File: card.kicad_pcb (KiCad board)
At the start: 2 copper layers, 38.6 x 52.3 mm, 91 parts, among them J1 Conn_01x20_Male, J2 HDMI_A, J3 Conn_01x20_Male, J4 USB_B_Micro, Q1 MMBT3906, Q3 MMBT3906, Q4 MMBT3904, SW1 SW_DPST_x2, U1 SPX3819-1.8, U2 IMP811REUS-T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

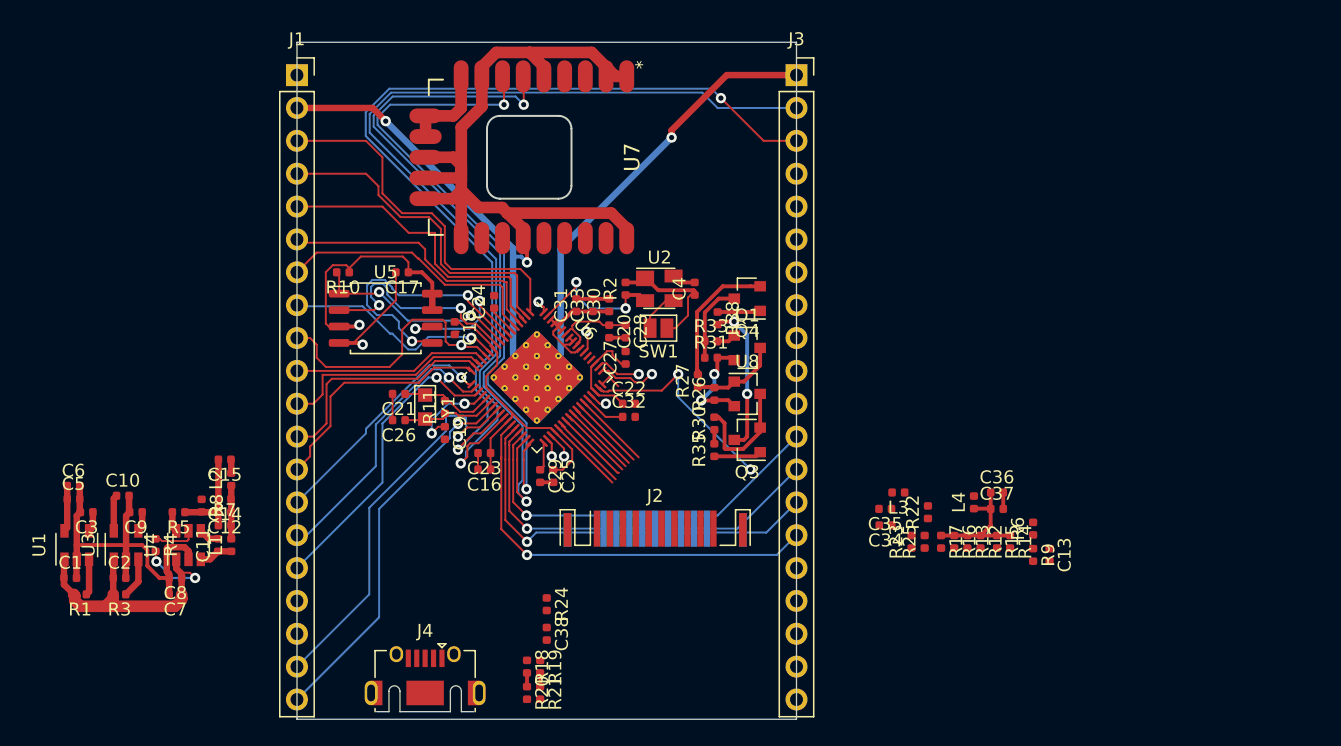
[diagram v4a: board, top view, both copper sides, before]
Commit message: removed USB power protection. did more routing
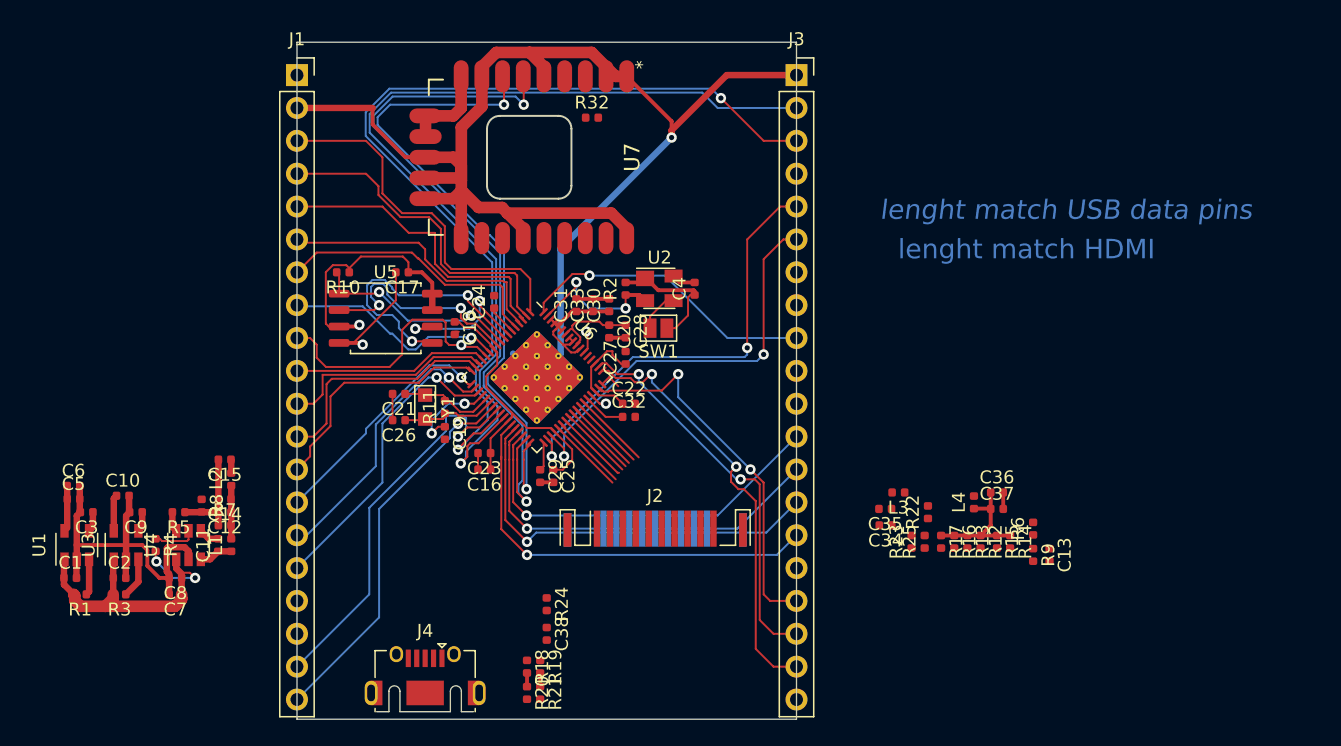
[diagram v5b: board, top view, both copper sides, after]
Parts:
- removed Q1, Q3: MMBT3906, Package_TO_SOT_SMD:SOT-23
- removed Q4: MMBT3904, Package_TO_SOT_SMD:SOT-23
- removed R26: 100k, Resistor_SMD:R_0402_1005Metric
- removed R27, R31: 10k, Resistor_SMD:R_0402_1005Metric
- removed R30: 0.5R, Resistor_SMD:R_0402_1005Metric
- removed R33, R35, R38: 510R, Resistor_SMD:R_0402_1005Metric
- removed U8: SLS2301, Package_TO_SOT_SMD:SOT-23
- added R32: 510R, Resistor_SMD:R_0402_1005Metric, F.Cu at (256.7, 62.5)
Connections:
- J3 pad 16: IR -> (no net)
- J3 pad 17: GND -> VOUT1
- J3 pad 18: VOUT1 -> AOR
- J3 pad 19: AOR -> AOL
- J3 pad 20: AOL -> GND
- J3 pad 4: USB2-VCC -> +5V
- J3 pad 8: (no net) -> GND
- J3 pad 9: (no net) -> IR
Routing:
- net HOST1_DP: track 1.48 -> 34.2 mm, vias 1 -> 2
- net HOST1_DM: track 2.04 -> 32.0 mm, vias 1 -> 2
- net AOL: track 4.47 -> 33.1 mm, vias 1 -> 2
- net AOR: track 3.58 -> 30.3 mm, vias 1 -> 2
- net GND: track 194.2 -> 169.5 mm, vias 4 -> 2
- net IR: track 0.96 -> 23.0 mm
- net VOUT1: track 16.5 -> 29.1 mm
- net Net-(Q3-Pad3): track 11.8 -> 0.00 mm, vias 2 -> 0
- net Net-(Q3-Pad2): track 9.18 -> 0.00 mm
- net +5V: track 33.0 -> 25.0 mm, vias 4 -> 2
- net Net-(Q1-Pad3): track 6.90 -> 0.00 mm
- net Net-(Q4-Pad3): track 6.22 -> 0.00 mm
- net Net-(Q3-Pad1): track 3.67 -> 0.00 mm
- net Net-(Q4-Pad1): track 3.32 -> 0.00 mm
- net Net-(Q1-Pad1): track 1.49 -> 0.00 mm
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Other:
- board text added: "lenght match HDMI"
- board text added: "lenght match USB data pins"

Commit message: started to add the HDMI port in the pcb
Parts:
- J2: footprint Connector_HDMI:HDMI_A_Contact_Technology_HDMI-19APL2_Horizontal -> C-SKY:HDMI-PCB
- moved J2 13.2 mm to (256.6, 106.4)
